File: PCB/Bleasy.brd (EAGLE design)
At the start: 33.6 x 62.2 mm, 14 parts, among them IC1 ATMEGA328-PU, Q1 8 MHz

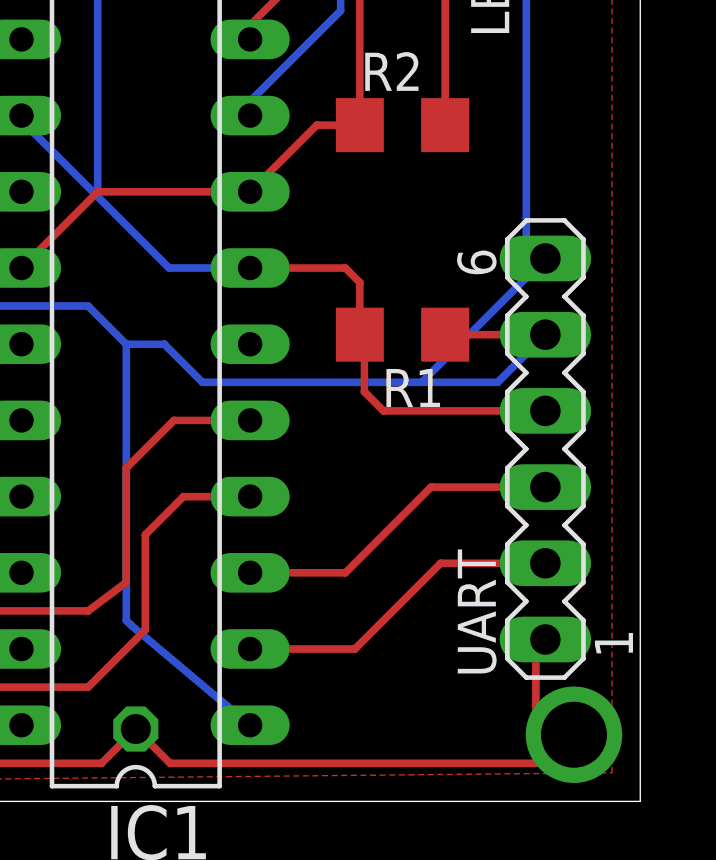
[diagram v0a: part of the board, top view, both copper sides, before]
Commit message: refactor(PCB): Moved UART pinheader some millimeters away from the drilling hole
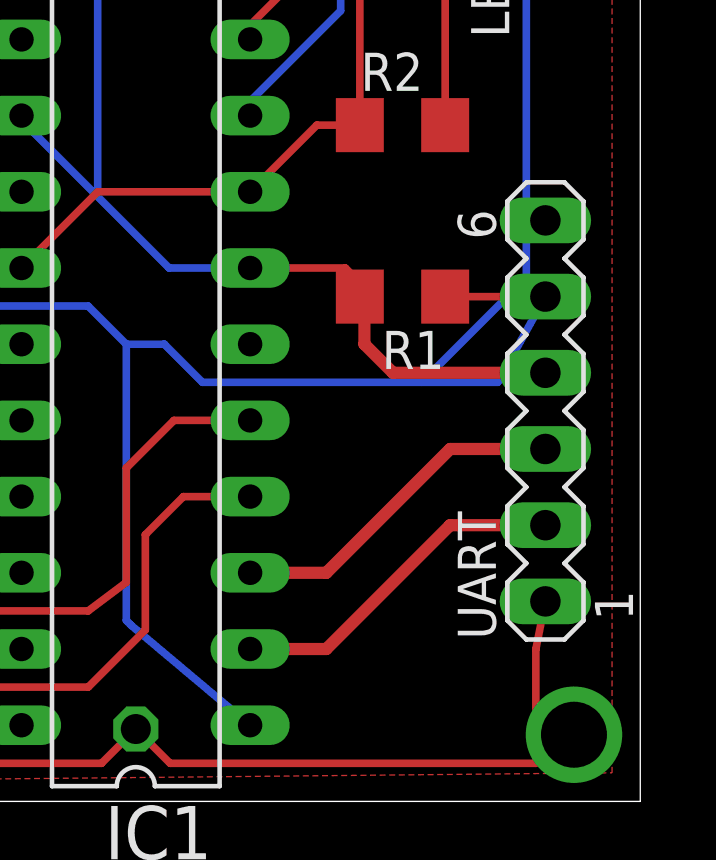
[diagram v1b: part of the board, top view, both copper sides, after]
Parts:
- moved R1 1.27 mm to (22.9, 16.8)
- moved UART 1.27 mm to (27.6, 13.0)
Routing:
- net +3V3: track 55.4 -> 54.0 mm
- net GND: track 163.0 -> 164.2 mm
- net RST: track 110.0 -> 111.1 mm
- net TX: track 11.0 -> 11.6 mm
- net RX: track 11.0 -> 11.6 mm
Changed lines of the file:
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@@
 <layers>
 <layer number="1" name="Top" color="4" fill="1" visible="yes" active="yes"/>
-<layer number="16" name="Bottom" color="1" fill="1" visible="yes" active="yes"/>
+<layer number="16" name="Bottom" color="1" fill="1" visible="no" active="yes"/>
 <layer number="17" name="Pads" color="2" fill="1" visible="yes" active="yes"/>
 <layer number="18" name="Vias" color="2" fill="1" visible="yes" active="yes"/>
@@
 <attribute name="OC_FARNELL" value="unknown" x="18.415" y="41.275" size="1.778" layer="27" display="off"/>
 </element>
-<element name="R1" library="resistor" package="R1206" value="100k" x="22.86" y="15.5575" rot="R180"/>
-<element name="UART" library="con-lstb" package="MA06-1" value="\" x="27.6225" y="11.7475" rot="R90">
-<attribute name="OC_NEWARK" value="unknown" x="27.6225" y="11.7475" size="1.778" layer="27" rot="R90" display="off"/>
-<attribute name="MPN" value="" x="27.6225" y="11.7475" size="1.778" layer="27" rot="R90" display="off"/>
-<attribute name="MF" value="" x="27.6225" y="11.7475" size="1.778" layer="27" rot="R90" display="off"/>
-<attribute name="OC_FARNELL" value="unknown" x="27.6225" y="11.7475" size="1.778" layer="27" rot="R90" display="off"/>
+<element name="R1" library="resistor" package="R1206" value="100k" x="22.86" y="16.8275" rot="R180"/>
+<element name="UART" library="con-lstb" package="MA06-1" value="\" x="27.6225" y="13.0175" rot="R90">
+<attribute name="OC_NEWARK" value="unknown" x="27.6225" y="13.0175" size="1.778" layer="27" rot="R90" display="off"/>
+<attribute name="MPN" value="" x="27.6225" y="13.0175" size="1.778" layer="27" rot="R90" display="off"/>
+<attribute name="MF" value="" x="27.6225" y="13.0175" size="1.778" layer="27" rot="R90" display="off"/>
+<attribute name="OC_FARNELL" value="unknown" x="27.6225" y="13.0175" size="1.778" layer="27" rot="R90" display="off"/>
 </element>
 <element name="R2" library="resistor" package="R1206" value="270" x="22.86" y="22.5425"/>
@@
 <wire x1="21.438" y1="35.408" x2="23.495" y2="37.465" width="0.254" layer="1"/>
 <wire x1="27.305" y1="1.27" x2="27.305" y2="5.08" width="0.254" layer="1"/>
-<wire x1="27.305" y1="5.08" x2="27.6225" y2="5.3975" width="0.254" layer="1"/>
+<wire x1="27.305" y1="5.08" x2="27.6225" y2="6.6675" width="0.254" layer="1"/>
 <wire x1="3.81" y1="22.86" x2="3.81" y2="17.78" width="0.254" layer="1"/>
 <wire x1="3.81" y1="17.78" x2="3.81" y2="16.51" width="0.254" layer="1"/>
@@
 <wire x1="17.78" y1="17.78" x2="20.955" y2="17.78" width="0.254" layer="1"/>
 <wire x1="20.955" y1="17.78" x2="21.438" y2="17.297" width="0.254" layer="1"/>
-<wire x1="21.438" y1="17.297" x2="21.438" y2="15.5575" width="0.254" layer="1"/>
-<wire x1="27.6225" y1="13.0175" x2="22.225" y2="13.0175" width="0.254" layer="1"/>
-<wire x1="22.225" y1="13.0175" x2="21.59" y2="13.6525" width="0.254" layer="1"/>
-<wire x1="21.59" y1="13.6525" x2="21.59" y2="15.088" width="0.254" layer="1"/>
-<wire x1="21.59" y1="15.088" x2="21.438" y2="15.5575" width="0.254" layer="1"/>
+<wire x1="21.438" y1="17.297" x2="21.438" y2="16.8275" width="0.254" layer="1"/>
+<wire x1="27.6225" y1="14.2875" x2="22.5425" y2="14.2875" width="0.4064" layer="1"/>
+<wire x1="22.5425" y1="14.2875" x2="21.59" y2="15.24" width="0.4064" layer="1"/>
+<wire x1="21.59" y1="15.24" x2="21.59" y2="16.6755" width="0.4064" layer="1"/>
+<wire x1="21.59" y1="16.6755" x2="21.438" y2="16.8275" width="0.4064" layer="1"/>
 </signal>
 <signal name="RST">
@@
 <wire x1="16.1925" y1="13.97" x2="23.495" y2="13.97" width="0.254" layer="16"/>
 <wire x1="23.495" y1="13.97" x2="26.035" y2="13.97" width="0.254" layer="16"/>
-<wire x1="26.035" y1="13.97" x2="27.6225" y2="15.5575" width="0.254" layer="16"/>
+<wire x1="26.035" y1="13.97" x2="27.6225" y2="16.8275" width="0.254" layer="16"/>
 <wire x1="22.62" y1="59.57" x2="22.62" y2="60.4025" width="0.254" layer="16"/>
 <wire x1="22.62" y1="60.4025" x2="23.1775" y2="60.96" width="0.254" layer="16"/>
@@
 <wire x1="26.9875" y1="45.085" x2="26.9875" y2="17.4625" width="0.254" layer="16"/>
 <wire x1="26.9875" y1="17.4625" x2="23.495" y2="13.97" width="0.254" layer="16"/>
-<wire x1="27.6225" y1="15.5575" x2="24.282" y2="15.5575" width="0.254" layer="1"/>
+<wire x1="27.6225" y1="16.8275" x2="24.282" y2="16.8275" width="0.254" layer="1"/>
 </signal>
 <signal name="RX">
 <contactref element="IC1" pad="2"/>
 <contactref element="UART" pad="2"/>
-<wire x1="27.6225" y1="7.9375" x2="24.13" y2="7.9375" width="0.254" layer="1"/>
-<wire x1="24.13" y1="7.9375" x2="21.2725" y2="5.08" width="0.254" layer="1"/>
-<wire x1="21.2725" y1="5.08" x2="17.78" y2="5.08" width="0.254" layer="1"/>
+<wire x1="27.6225" y1="9.2075" x2="24.4475" y2="9.2075" width="0.4064" layer="1"/>
+<wire x1="24.4475" y1="9.2075" x2="20.32" y2="5.08" width="0.4064" layer="1"/>
+<wire x1="20.32" y1="5.08" x2="17.78" y2="5.08" width="0.4064" layer="1"/>
 </signal>
 <signal name="TX">
 <contactref element="IC1" pad="3"/>
 <contactref element="UART" pad="3"/>
-<wire x1="27.6225" y1="10.4775" x2="23.8125" y2="10.4775" width="0.254" layer="1"/>
-<wire x1="23.8125" y1="10.4775" x2="20.955" y2="7.62" width="0.254" layer="1"/>
-<wire x1="20.955" y1="7.62" x2="17.78" y2="7.62" width="0.254" layer="1"/>
+<wire x1="27.6225" y1="11.7475" x2="24.4475" y2="11.7475" width="0.4064" layer="1"/>
+<wire x1="24.4475" y1="11.7475" x2="20.32" y2="7.62" width="0.4064" layer="1"/>
+<wire x1="20.32" y1="7.62" x2="17.78" y2="7.62" width="0.4064" layer="1"/>
 </signal>
 <signal name="MISO">

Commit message: Renamed project
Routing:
- net RST: track 111.1 -> 108.6 mm
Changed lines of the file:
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@@
 <layers>
 <layer number="1" name="Top" color="4" fill="1" visible="yes" active="yes"/>
-<layer number="16" name="Bottom" color="1" fill="1" visible="no" active="yes"/>
+<layer number="16" name="Bottom" color="1" fill="1" visible="yes" active="yes"/>
 <layer number="17" name="Pads" color="2" fill="1" visible="yes" active="yes"/>
 <layer number="18" name="Vias" color="2" fill="1" visible="yes" active="yes"/>
@@
 <layer number="27" name="tValues" color="7" fill="1" visible="yes" active="yes"/>
 <layer number="28" name="bValues" color="7" fill="1" visible="yes" active="yes"/>
-<layer number="29" name="tStop" color="7" fill="3" visible="no" active="yes"/>
-<layer number="30" name="bStop" color="7" fill="6" visible="no" active="yes"/>
-<layer number="31" name="tCream" color="7" fill="4" visible="no" active="yes"/>
-<layer number="32" name="bCream" color="7" fill="5" visible="no" active="yes"/>
-<layer number="33" name="tFinish" color="6" fill="3" visible="no" active="yes"/>
-<layer number="34" name="bFinish" color="6" fill="6" visible="no" active="yes"/>
-<layer number="35" name="tGlue" color="7" fill="4" visible="no" active="yes"/>
-<layer number="36" name="bGlue" color="7" fill="5" visible="no" active="yes"/>
-<layer number="37" name="tTest" color="7" fill="1" visible="no" active="yes"/>
-<layer number="38" name="bTest" color="7" fill="1" visible="no" active="yes"/>
-<layer number="39" name="tKeepout" color="4" fill="11" visible="no" active="yes"/>
-<layer number="40" name="bKeepout" color="1" fill="11" visible="no" active="yes"/>
-<layer number="41" name="tRestrict" color="4" fill="10" visible="no" active="yes"/>
-<layer number="42" name="bRestrict" color="1" fill="10" visible="no" active="yes"/>
-<layer number="43" name="vRestrict" color="2" fill="10" visible="no" active="yes"/>
-<layer number="44" name="Drills" color="7" fill="1" visible="no" active="yes"/>
-<layer number="45" name="Holes" color="7" fill="1" visible="no" active="yes"/>
-<layer number="46" name="Milling" color="3" fill="1" visible="no" active="yes"/>
-<layer number="47" name="Measures" color="7" fill="1" visible="no" active="yes"/>
-<layer number="48" name="Document" color="7" fill="1" visible="no" active="yes"/>
-<layer number="49" name="Reference" color="7" fill="1" visible="no" active="yes"/>
+<layer number="29" name="tStop" color="7" fill="3" visible="yes" active="yes"/>
+<layer number="30" name="bStop" color="7" fill="6" visible="yes" active="yes"/>
+<layer number="31" name="tCream" color="7" fill="4" visible="yes" active="yes"/>
+<layer number="32" name="bCream" color="7" fill="5" visible="yes" active="yes"/>
+<layer number="33" name="tFinish" color="6" fill="3" visible="yes" active="yes"/>
+<layer number="34" name="bFinish" color="6" fill="6" visible="yes" active="yes"/>
+<layer number="35" name="tGlue" color="7" fill="4" visible="yes" active="yes"/>
+<layer number="36" name="bGlue" color="7" fill="5" visible="yes" active="yes"/>
+<layer number="37" name="tTest" color="7" fill="1" visible="yes" active="yes"/>
+<layer number="38" name="bTest" color="7" fill="1" visible="yes" active="yes"/>
+<layer number="39" name="tKeepout" color="4" fill="11" visible="yes" active="yes"/>
+<layer number="40" name="bKeepout" color="1" fill="11" visible="yes" active="yes"/>
+<layer number="41" name="tRestrict" color="4" fill="10" visible="yes" active="yes"/>
+<layer number="42" name="bRestrict" color="1" fill="10" visible="yes" active="yes"/>
+<layer number="43" name="vRestrict" color="2" fill="10" visible="yes" active="yes"/>
+<layer number="44" name="Drills" color="7" fill="1" visible="yes" active="yes"/>
+<layer number="45" name="Holes" color="7" fill="1" visible="yes" active="yes"/>
+<layer number="46" name="Milling" color="3" fill="1" visible="yes" active="yes"/>
+<layer number="47" name="Measures" color="7" fill="1" visible="yes" active="yes"/>
+<layer number="48" name="Document" color="7" fill="1" visible="yes" active="yes"/>
+<layer number="49" name="Reference" color="7" fill="1" visible="yes" active="yes"/>
 <layer number="50" name="dxf" color="7" fill="1" visible="no" active="no"/>
-<layer number="51" name="tDocu" color="7" fill="1" visible="no" active="yes"/>
-<layer number="52" name="bDocu" color="7" fill="1" visible="no" active="yes"/>
+<layer number="51" name="tDocu" color="7" fill="1" visible="yes" active="yes"/>
+<layer number="52" name="bDocu" color="7" fill="1" visible="yes" active="yes"/>
 <layer number="90" name="Modules" color="5" fill="1" visible="no" active="no"/>
 <layer number="91" name="Nets" color="2" fill="1" visible="no" active="no"/>
@@
 <wire x1="2.54" y1="43.4975" x2="-0.635" y2="43.4975" width="0.254" layer="1"/>
 <wire x1="-0.635" y1="43.4975" x2="-0.635" y2="60.0075" width="0.254" layer="1"/>
-<polygon width="0.254" layer="1" isolate="0.254" thermals="no">
+<polygon width="0.8128" layer="1" isolate="0.254" thermals="no">
 <vertex x="-2.2225" y="61.2775"/>
 <vertex x="-2.2225" y="0.635"/>
@@
 <wire x1="20.955" y1="17.78" x2="21.438" y2="17.297" width="0.254" layer="1"/>
 <wire x1="21.438" y1="17.297" x2="21.438" y2="16.8275" width="0.254" layer="1"/>
-<wire x1="27.6225" y1="14.2875" x2="22.5425" y2="14.2875" width="0.4064" layer="1"/>
-<wire x1="22.5425" y1="14.2875" x2="21.59" y2="15.24" width="0.4064" layer="1"/>
-<wire x1="21.59" y1="15.24" x2="21.59" y2="16.6755" width="0.4064" layer="1"/>
+<wire x1="27.6225" y1="14.2875" x2="22.5425" y2="14.2875" width="0.254" layer="1"/>
+<wire x1="22.5425" y1="14.2875" x2="21.59" y2="15.24" width="0.254" layer="1"/>
+<wire x1="21.59" y1="15.24" x2="21.59" y2="16.6755" width="0.254" layer="1"/>
 <wire x1="21.59" y1="16.6755" x2="21.438" y2="16.8275" width="0.4064" layer="1"/>
 </signal>
@@
 <wire x1="13.6525" y1="15.24" x2="14.9225" y2="15.24" width="0.254" layer="16"/>
 <wire x1="14.9225" y1="15.24" x2="16.1925" y2="13.97" width="0.254" layer="16"/>
-<wire x1="16.1925" y1="13.97" x2="23.495" y2="13.97" width="0.254" layer="16"/>
-<wire x1="23.495" y1="13.97" x2="26.035" y2="13.97" width="0.254" layer="16"/>
-<wire x1="26.035" y1="13.97" x2="27.6225" y2="16.8275" width="0.254" layer="16"/>
+<wire x1="16.1925" y1="13.97" x2="24.765" y2="13.97" width="0.254" layer="16"/>
 <wire x1="22.62" y1="59.57" x2="22.62" y2="60.4025" width="0.254" layer="16"/>
 <wire x1="22.62" y1="60.4025" x2="23.1775" y2="60.96" width="0.254" layer="16"/>
@@
 <wire x1="26.9875" y1="60.96" x2="28.8925" y2="59.055" width="0.254" layer="16"/>
 <wire x1="28.8925" y1="59.055" x2="28.8925" y2="46.99" width="0.254" layer="16"/>
-<wire x1="28.8925" y1="46.99" x2="26.9875" y2="45.085" width="0.254" layer="16"/>
-<wire x1="26.9875" y1="45.085" x2="26.9875" y2="17.4625" width="0.254" layer="16"/>
-<wire x1="26.9875" y1="17.4625" x2="23.495" y2="13.97" width="0.254" layer="16"/>
+<wire x1="28.8925" y1="46.99" x2="26.67" y2="44.7675" width="0.254" layer="16"/>
 <wire x1="27.6225" y1="16.8275" x2="24.282" y2="16.8275" width="0.254" layer="1"/>
+<wire x1="24.765" y1="13.97" x2="27.6225" y2="16.8275" width="0.254" layer="16"/>
+<wire x1="27.6225" y1="16.8275" x2="26.3525" y2="16.8275" width="0.254" layer="16"/>
+<wire x1="26.3525" y1="16.8275" x2="25.4" y2="17.78" width="0.254" layer="16"/>
+<wire x1="25.4" y1="17.78" x2="25.4" y2="29.21" width="0.254" layer="16"/>
+<wire x1="25.4" y1="29.21" x2="26.67" y2="30.48" width="0.254" layer="16"/>
+<wire x1="26.67" y1="30.48" x2="26.67" y2="44.7675" width="0.254" layer="16"/>
 </signal>
 <signal name="RX">
 <contactref element="IC1" pad="2"/>
 <contactref element="UART" pad="2"/>
-<wire x1="27.6225" y1="9.2075" x2="24.4475" y2="9.2075" width="0.4064" layer="1"/>
-<wire x1="24.4475" y1="9.2075" x2="20.32" y2="5.08" width="0.4064" layer="1"/>
-<wire x1="20.32" y1="5.08" x2="17.78" y2="5.08" width="0.4064" layer="1"/>
+<wire x1="27.6225" y1="9.2075" x2="24.4475" y2="9.2075" width="0.254" layer="1"/>
+<wire x1="24.4475" y1="9.2075" x2="20.32" y2="5.08" width="0.254" layer="1"/>
+<wire x1="20.32" y1="5.08" x2="17.78" y2="5.08" width="0.254" layer="1"/>
 </signal>
 <signal name="TX">
 <contactref element="IC1" pad="3"/>
 <contactref element="UART" pad="3"/>
-<wire x1="27.6225" y1="11.7475" x2="24.4475" y2="11.7475" width="0.4064" layer="1"/>
-<wire x1="24.4475" y1="11.7475" x2="20.32" y2="7.62" width="0.4064" layer="1"/>
-<wire x1="20.32" y1="7.62" x2="17.78" y2="7.62" width="0.4064" layer="1"/>
+<wire x1="27.6225" y1="11.7475" x2="24.4475" y2="11.7475" width="0.254" layer="1"/>
+<wire x1="24.4475" y1="11.7475" x2="20.32" y2="7.62" width="0.254" layer="1"/>
+<wire x1="20.32" y1="7.62" x2="17.78" y2="7.62" width="0.254" layer="1"/>
 </signal>
 <signal name="MISO">
